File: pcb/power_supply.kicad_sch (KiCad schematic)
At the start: 17 parts, among them U1 AMS1117-3.3, U2 ADP2303ARDZ-5.0

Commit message: Added part numbers for assembly
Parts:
- C1: LCSC (none) -> C440198
- C3: LCSC (none) -> C16780
- D1, D4: LCSC (none) -> C222519
- D3: LCSC (none) -> C78809
- D5, D6: LCSC (none) -> C72043
- F1: LCSC (none) -> C122965
- L1: LCSC (none) -> C2847561
- R1: LCSC (none) -> C25086
- R3, R4: LCSC (none) -> C4177
- U2: LCSC (none) -> C659153
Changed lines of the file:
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@@
+      (effects (font (size 1.27 1.27)) hide)
+    )
+    (property "LCSC" "C122965" (id 4) (at 60.96 62.23 0)
       (effects (font (size 1.27 1.27)) hide)
     )
@@
     )
     (property "Datasheet" "~" (id 3) (at 143.51 69.85 0)
+      (effects (font (size 1.27 1.27)) hide)
+    )
+    (property "LCSC" "C16780" (id 4) (at 143.51 69.85 0)
       (effects (font (size 1.27 1.27)) hide)
     )
@@
       (effects (font (size 1.27 1.27)) hide)
     )
+    (property "LCSC" "C222519" (id 4) (at 73.66 62.23 0)
+      (effects (font (size 1.27 1.27)) hide)
+    )
     (pin "1")
     (pin "2")
@@
       (effects (font (size 1.27 1.27)) hide)
     )
+    (property "LCSC" "C440198" (id 4) (at 82.55 64.77 0)
+      (effects (font (size 1.27 1.27)) hide)
+    )
     (pin "1")
     (pin "2")
@@
     )
     (property "Datasheet" "~" (id 3) (at 132.08 120.65 0)
+      (effects (font (size 1.27 1.27)) hide)
+    )
+    (property "LCSC" "C4177" (id 4) (at 132.08 120.65 0)
       (effects (font (size 1.27 1.27)) hide)
     )
@@
       (effects (font (size 1.27 1.27)) hide)
     )
+    (property "LCSC" "C25086" (id 4) (at 92.71 69.85 0)
+      (effects (font (size 1.27 1.27)) hide)
+    )
     (pin "1")
     (pin "2")
@@
     )
     (property "Datasheet" "~" (id 3) (at 142.24 120.65 0)
+      (effects (font (size 1.27 1.27)) hide)
+    )
+    (property "LCSC" "C4177" (id 4) (at 142.24 120.65 0)
       (effects (font (size 1.27 1.27)) hide)
     )
@@
       (effects (font (size 1.27 1.27)) hide)
     )
+    (property "LCSC" "C2847561" (id 4) (at 135.89 67.31 0)
+      (effects (font (size 1.27 1.27)) hide)
+    )
     (pin "1")
     (pin "2")
@@
     )
     (property "Datasheet" "~" (id 3) (at 132.08 127 0)
+      (effects (font (size 1.27 1.27)) hide)
+    )
+    (property "LCSC" "C72043" (id 4) (at 132.08 127 0)
       (effects (font (size 1.27 1.27)) hide)
     )
@@
     )
     (property "Datasheet" "https://www.analog.com/media/en/technical-documentation/data-sheets/ADP2302_2303.pdf" (id 3) (at 102.87 52.07 0)
+      (effects (font (size 1.27 1.27)) hide)
+    )
+    (property "LCSC" "C659153" (id 4) (at 107.95 67.31 0)
       (effects (font (size 1.27 1.27)) hide)
     )
@@
       (effects (font (size 1.27 1.27)) hide)
     )
+    (property "LCSC" "C222519" (id 4) (at 125.73 71.12 0)
+      (effects (font (size 1.27 1.27)) hide)
+    )
     (pin "1")
     (pin "2")
@@
       (effects (font (size 1.27 1.27)) hide)
     )
+    (property "LCSC" "C78809" (id 4) (at 67.31 66.04 0)
+      (effects (font (size 1.27 1.27)) hide)
+    )
     (pin "1")
     (pin "2")
@@
       (effects (font (size 1.27 1.27)) hide)
     )
+    (property "LCSC" "C72043" (id 4) (at 142.24 127 0)
+      (effects (font (size 1.27 1.27)) hide)
+    )

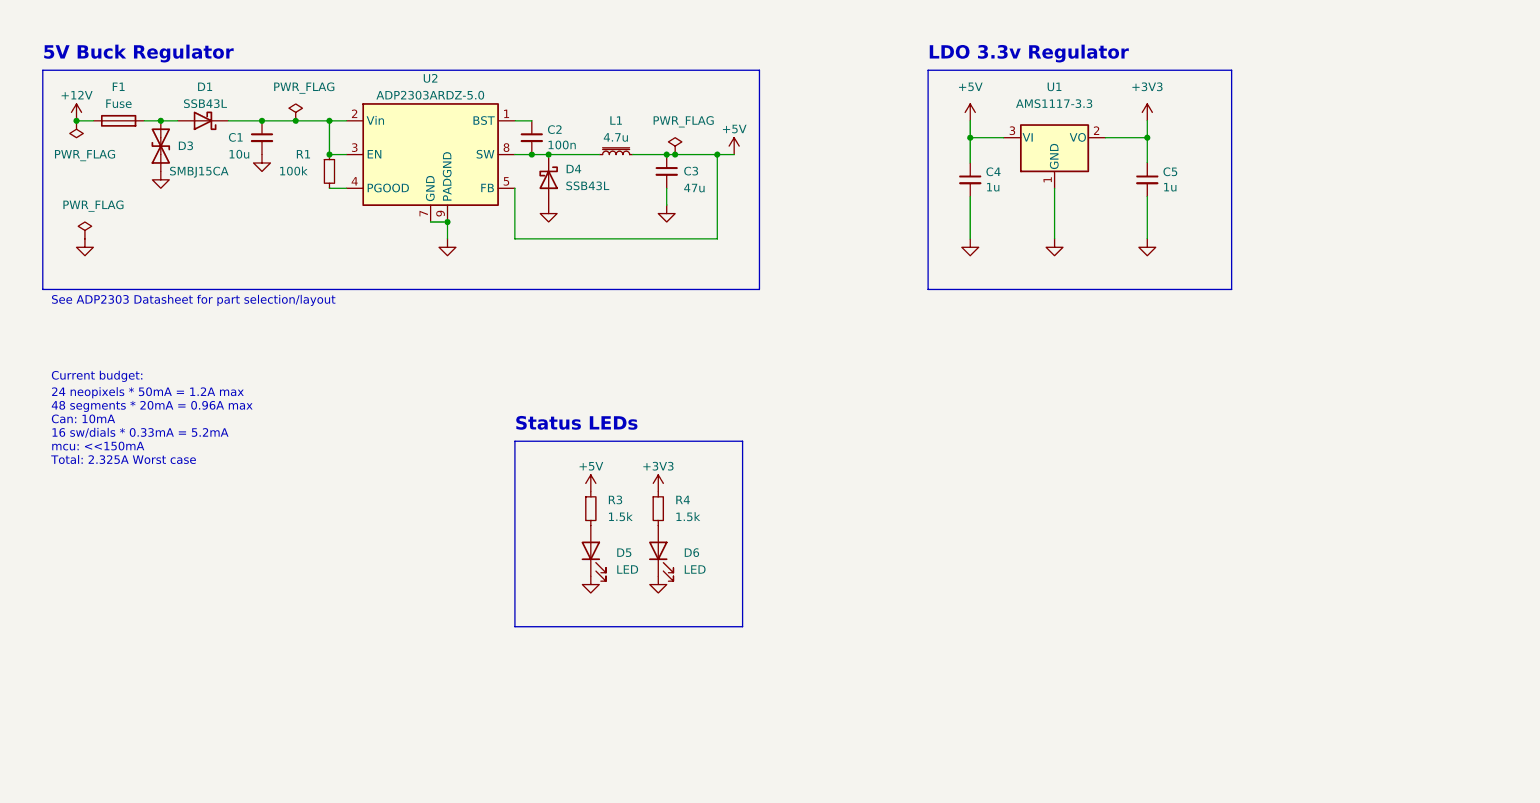
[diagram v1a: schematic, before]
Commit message: Started work on discrete led displays
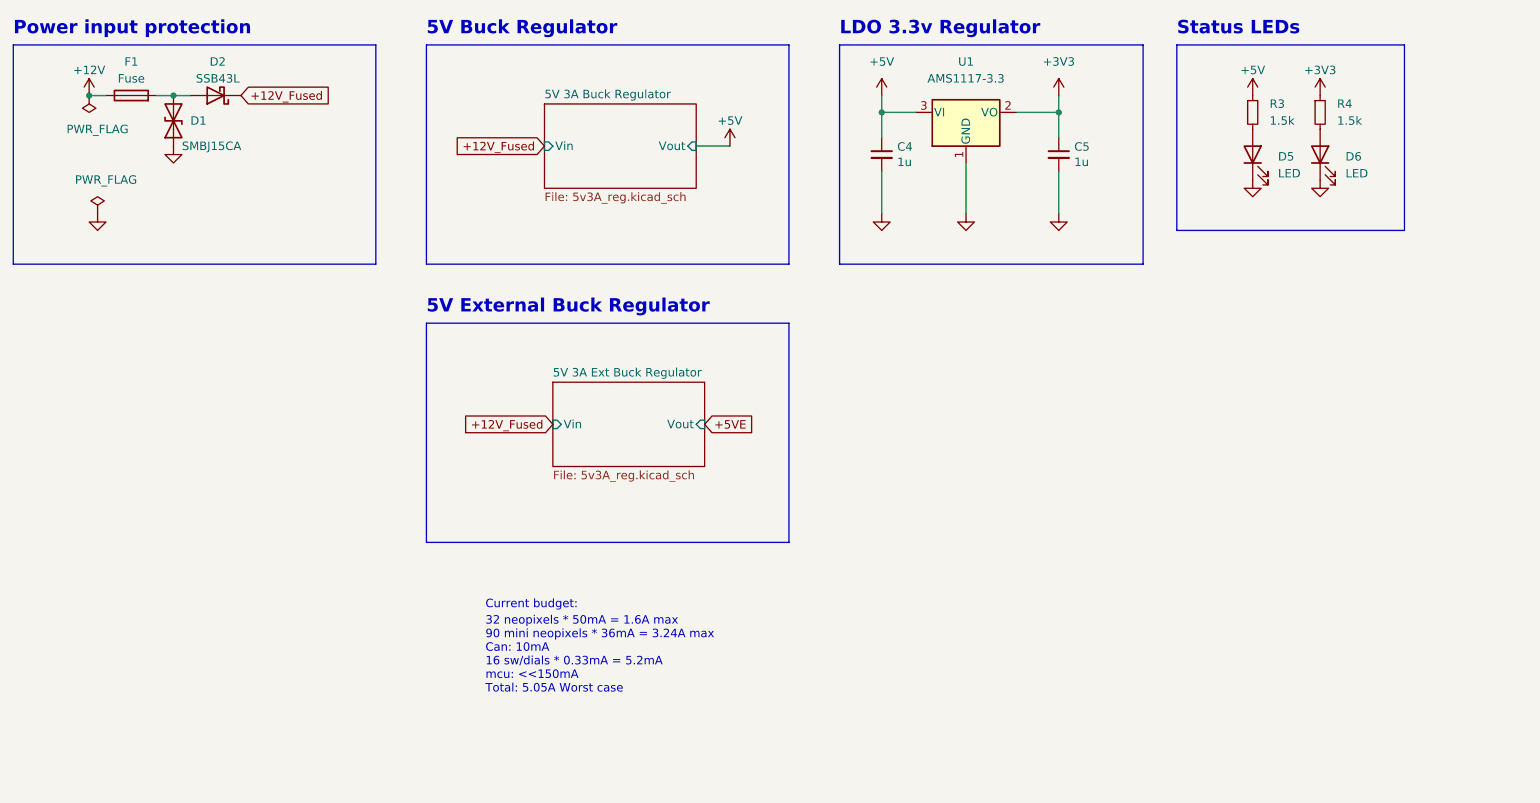
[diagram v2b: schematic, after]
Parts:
- removed C1: 10u, Capacitor_SMD:C_0805_2012Metric, symbol Device:C_Small
- removed C2: 100n, Capacitor_SMD:C_0402_1005Metric, symbol Device:C_Small
- removed C3: 47u, Capacitor_SMD:C_0805_2012Metric, symbol Device:C_Small
- removed D1, D4: SSB43L, Diode_SMD:D_SMB, symbol Device:D_Schottky
- removed D3: SMBJ15CA, Diode_SMD:D_SMB, symbol Device:D_TVS
- removed L1: 4.7u, Inductor_SMD:L_12x12mm_H6mm, symbol Device:L_Iron_Small
- removed R1: 100k, Resistor_SMD:R_0402_1005Metric, symbol Device:R_Small
- removed U2: ADP2303ARDZ-5.0, Package_SO:SOIC-8-1EP_3.9x4.9mm_P1.27mm_EP2.29x3mm, symbol Regulator_Switching:ADP2303ARDZ-5.0
- added D1: SMBJ15CA, Diode_SMD:D_SMB, symbol Device:D_TVS
- added D2: SSB43L, Diode_SMD:D_SMB, symbol Device:D_Schottky
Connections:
- net GND: now also D1.1 (A1)
- net at F1.2: now also D1.2 (A2), D2.2 (A)
- new net +12V_Fused: D2.1 (K)
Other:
- added sheet 5V 3A Buck Regulator (5v3A_reg.kicad_sch)
- added sheet 5V 3A Ext Buck Regulator (5v3A_reg.kicad_sch)
- note added: "32 neopixels * 50mA = 1.6A max 90 mini neopixels * 36mA = 3.24A max Can: 10mA 16 sw/dials * 0.33mA = 5.2mA mcu: <<150mA Total: 5.05A Worst case"
- note added: "5V External Buck Regulator"
- note added: "Power input protection"
- note removed: "24 neopixels * 50mA = 1.2A max 48 segments * 20mA = 0.96A max Can: 10mA 16 sw/dials * 0.33mA = 5.2mA mcu: <<150mA Total: 2.325A Worst case"
- note removed: "See ADP2303 Datasheet for part selection/layout"
- moved on the sheet: C4, C5, D5, D6, R3, R4, U1

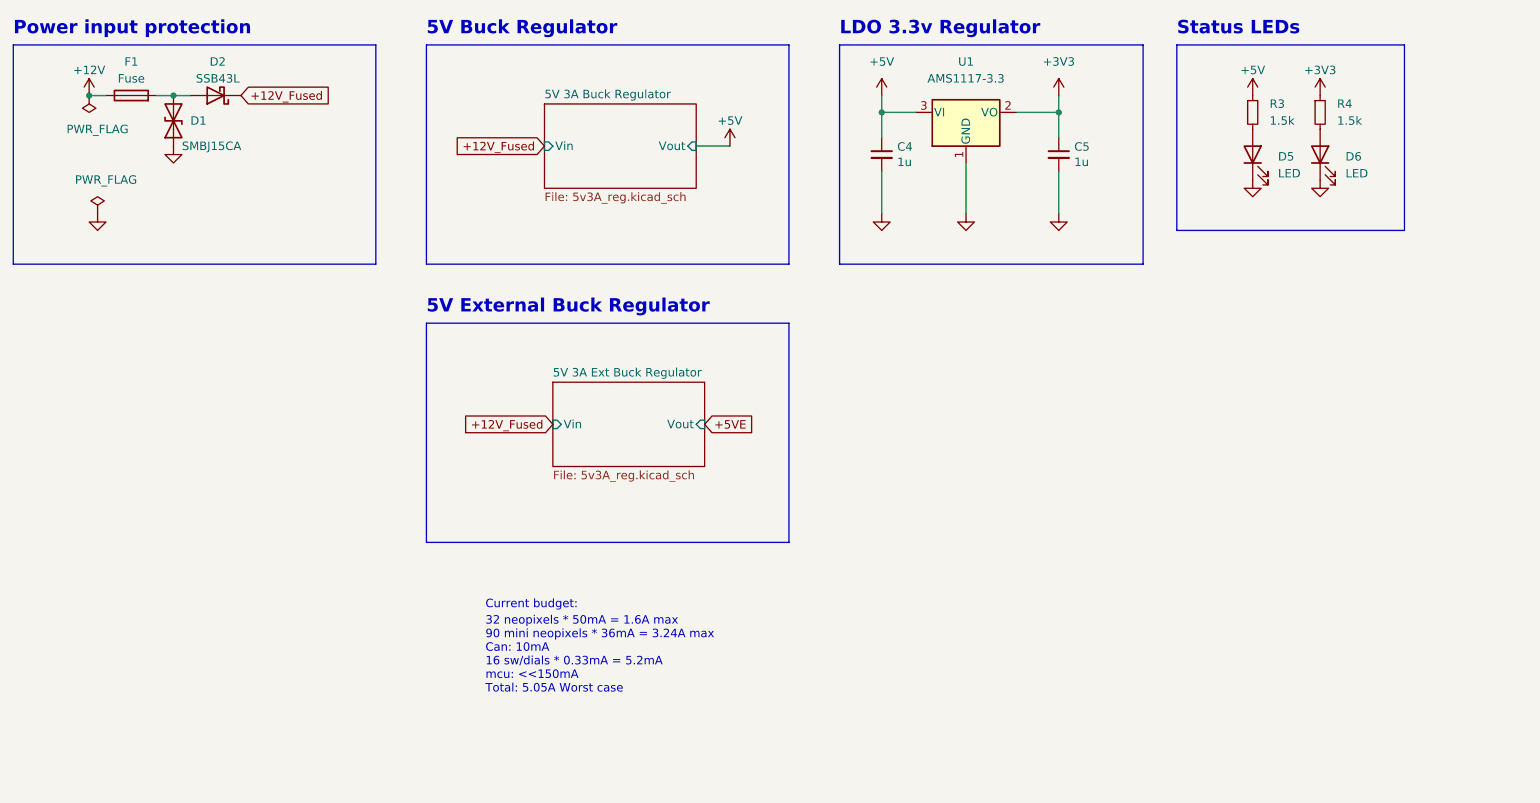
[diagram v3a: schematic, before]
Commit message: Fix kikad 7 schematic issues
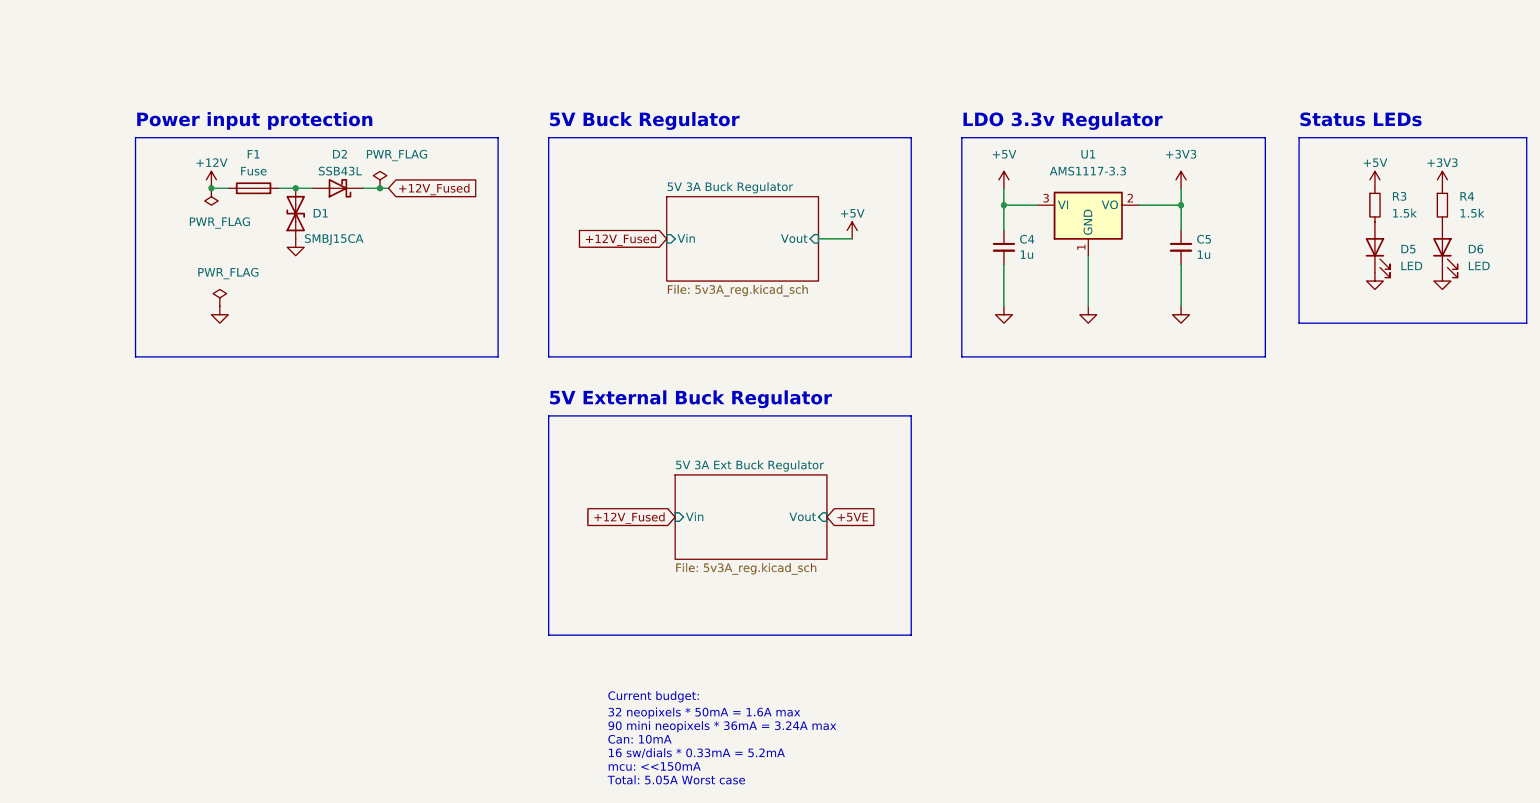
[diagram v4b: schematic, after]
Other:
- moved on the sheet: C4, C5, D1, D2, D5, D6, F1, R3, R4, U1
